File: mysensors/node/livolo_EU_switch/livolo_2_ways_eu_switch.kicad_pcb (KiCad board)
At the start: 2 copper layers, 43.4 x 43.5 mm, 50 parts, among them CON1 AVR-ISP-6, IC1 ATMEGA328P-AU, P1 Sense Pad 1, P2 Sense Pad 2, P3 ANTENNA, P4 Power Board, U1 MIC5205-3.3, U2 MCP16301, U3 TTP223, U4 TTP223, U5 RFM69CW, U6 AT25DF512C-SSHN-B, U7 ATSHA204A

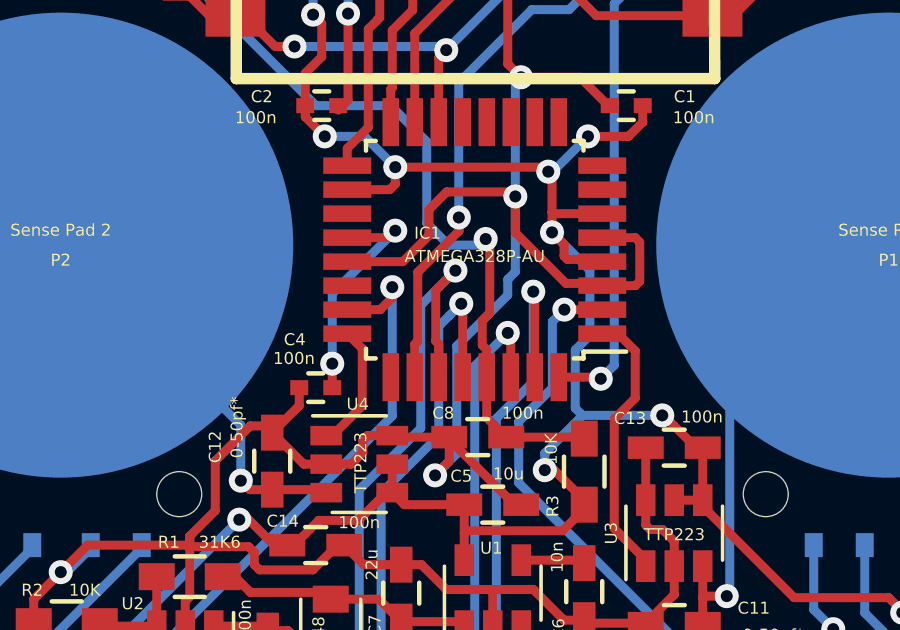
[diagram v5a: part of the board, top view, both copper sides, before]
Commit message: [livolo_EU_switch] cleaned up schematic
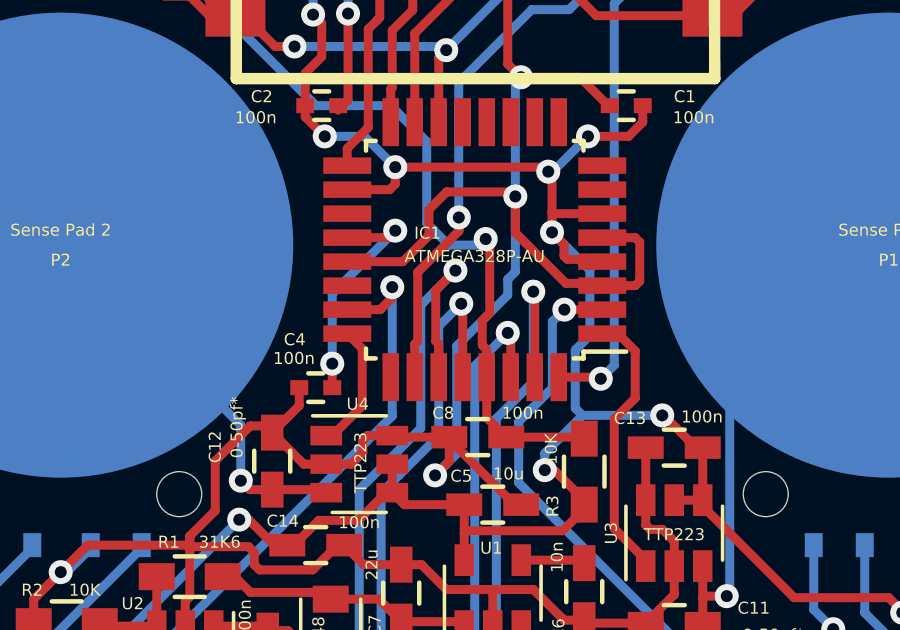
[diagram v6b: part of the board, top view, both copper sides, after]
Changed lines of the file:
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@@
     (thickness 1.6)
     (drawings 15)
-    (tracks 590)
+    (tracks 589)
     (zones 0)
     (modules 50)
@@
     (tags SOT-23-6)
     (attr smd)
-    (fp_text reference U2 (at -1.85 1.75 360) (layer F.SilkS)
+    (fp_text reference U2 (at -1.85 1.75) (layer F.SilkS)
       (effects (font (size 0.4 0.4) (thickness 0.1)))
     )
@@
   (gr_line (start 151.552777 113.515554) (end 131.572683 113.515554) (layer Edge.Cuts) (width 0.1))
   (gr_line (start 164.116018 81.426312) (end 164.116018 102.125387) (layer Edge.Cuts) (width 0.1))
-  (segment (start 146.7 92.7) (end 146.625001 92.625001) (width 0.3) (layer F.Cu) (net 1))
-  (segment (start 146.625001 92.625001) (end 145.539999 92.625001) (width 0.3) (layer F.Cu) (net 1))
+  (segment (start 146.7 92.7) (end 146.625001 92.625001) (width 0.3) (layer F.Cu) (net 1) (status 30))
+  (segment (start 146.625001 92.625001) (end 145.539999 92.625001) (width 0.3) (layer F.Cu) (net 1) (status 10))
   (segment (start 145.539999 92.625001) (end 145.426047 92.511049) (width 0.3) (layer F.Cu) (net 1))
   (segment (start 145.426047 92.511049) (end 145.426047 92.123951) (width 0.3) (layer F.Cu) (net 1))
@@
   (segment (start 137.250001 101.324999) (end 136.425 102.15) (width 0.3) (layer F.Cu) (net 1) (status 20))
   (segment (start 150.05 100.65) (end 150.05 98.9) (width 0.3) (layer F.Cu) (net 1) (status 30))
-  (segment (start 152.85 72.25) (end 152.15 72.25) (width 0.3) (layer F.Cu) (net 2))
-  (segment (start 152.15 72.25) (end 150.72104 72.25) (width 0.3) (layer F.Cu) (net 2))
+  (segment (start 152.85 72.25) (end 152.15 72.25) (width 0.3) (layer F.Cu) (net 2) (status 10))
+  (segment (start 152.15 72.25) (end 150.72104 72.25) (width 0.3) (layer F.Cu) (net 2) (status 20))
   (segment (start 154.7 77.600002) (end 152.15 75.050002) (width 0.3) (layer F.Cu) (net 2))
   (segment (start 152.15 75.050002) (end 152.15 72.25) (width 0.3) (layer F.Cu) (net 2))
-  (segment (start 145.491456 93.425001) (end 146.625001 93.425001) (width 0.3) (layer F.Cu) (net 2))
+  (segment (start 145.491456 93.425001) (end 146.625001 93.425001) (width 0.3) (layer F.Cu) (net 2) (status 20))
   (segment (start 143.802464 90.525717) (end 143.802464 91.736009) (width 0.3) (layer F.Cu) (net 2))
   (segment (start 143.802464 91.736009) (end 145.491456 93.425001) (width 0.3) (layer F.Cu) (net 2))
-  (segment (start 146.625001 93.425001) (end 146.7 93.5) (width 0.3) (layer F.Cu) (net 2))
+  (segment (start 146.625001 93.425001) (end 146.7 93.5) (width 0.3) (layer F.Cu) (net 2) (status 30))
   (segment (start 147.950001 92.050001) (end 147.950001 93.349999) (width 0.3) (layer F.Cu) (net 2))
   (segment (start 147.950001 93.349999) (end 147.8 93.5) (width 0.3) (layer F.Cu) (net 2))
-  (segment (start 146.7 93.5) (end 147.8 93.5) (width 0.3) (layer F.Cu) (net 2))
+  (segment (start 146.7 93.5) (end 147.8 93.5) (width 0.3) (layer F.Cu) (net 2) (status 10))
   (segment (start 147.8 91.9) (end 147.950001 92.050001) (width 0.3) (layer F.Cu) (net 2))
   (segment (start 146.7 91.9) (end 147.8 91.9) (width 0.3) (layer F.Cu) (net 2) (status 10))
-  (segment (start 138.2 92.7) (end 140.053139 92.7) (width 0.3) (layer F.Cu) (net 2))
+  (segment (start 138.2 92.7) (end 140.053139 92.7) (width 0.3) (layer F.Cu) (net 2) (status 10))
   (segment (start 140.053139 92.7) (end 140.925 91.828139) (width 0.3) (layer F.Cu) (net 2))
   (segment (start 140.925 91.828139) (end 140.925 90.963954) (width 0.3) (layer F.Cu) (net 2))
@@
   (segment (start 137.65 103.95) (end 139.25 103.95) (width 0.3) (layer F.Cu) (net 5) (status 10))
   (segment (start 139.25 103.95) (end 140 104.7) (width 0.3) (layer F.Cu) (net 5) (status 20))
-  (segment (start 142.85 96.55) (end 142.85 95.632681) (width 0.3) (layer F.Cu) (net 6))
+  (segment (start 142.85 96.55) (end 142.85 95.632681) (width 0.3) (layer F.Cu) (net 6) (status 10))
   (segment (start 142.85 95.632681) (end 142.699989 95.48267) (width 0.3) (layer F.Cu) (net 6))
   (segment (start 142.699989 95.48267) (end 142.699989 94.664027) (width 0.3) (layer F.Cu) (net 6))
@@
   (segment (start 135.7 100.3) (end 137.4 100.3) (width 0.3) (layer F.Cu) (net 11) (status 30))
   (segment (start 137.4 100.3) (end 137.5 100.4) (width 0.3) (layer F.Cu) (net 11) (status 30))
-  (segment (start 154.415 79.5) (end 154.415 80.575) (width 0.3) (layer F.Cu) (net 12))
-  (segment (start 151.07378 84.50122) (end 150.37226 84.50122) (width 0.3) (layer F.Cu) (net 12))
+  (segment (start 154.415 79.5) (end 154.415 80.575) (width 0.3) (layer F.Cu) (net 12) (status 10))
+  (segment (start 151.07378 84.50122) (end 150.37226 84.50122) (width 0.3) (layer F.Cu) (net 12) (status 30))
   (segment (start 154.415 80.575) (end 154.250001 80.739999) (width 0.3) (layer F.Cu) (net 12))
   (segment (start 154.250001 80.739999) (end 154.250001 82.510001) (width 0.3) (layer F.Cu) (net 12))
   (segment (start 154.250001 82.510001) (end 153.860002 82.9) (width 0.3) (layer F.Cu) (net 12))
   (segment (start 153.860002 82.9) (end 152.675 82.9) (width 0.3) (layer F.Cu) (net 12))
-  (segment (start 152.675 82.9) (end 151.07378 84.50122) (width 0.3) (layer F.Cu) (net 12))
+  (segment (start 152.675 82.9) (end 151.07378 84.50122) (width 0.3) (layer F.Cu) (net 12) (status 20))
   (segment (start 128.450018 81.600004) (end 128.000012 82.05001) (width 0.3) (layer B.Cu) (net 12))
   (segment (start 129.55001 82.05001) (end 128.000012 82.05001) (width 0.3) (layer F.Cu) (net 12) (status 10))
@@
   (segment (start 144.45 93.75) (end 144.4 93.7) (width 0.3) (layer F.Cu) (net 28))
   (via (at 144.4 93.7) (size 0.8) (drill 0.4) (layers F.Cu B.Cu) (net 28))
-  (segment (start 141.249969 94.853552) (end 141.600036 94.503485) (width 0.3) (layer B.Cu) (net 29))
+  (segment (start 141.249969 94.853552) (end 142.000035 94.103486) (width 0.3) (layer B.Cu) (net 29))
   (segment (start 142.05 94.153451) (end 142.000035 94.103486) (width 0.3) (layer F.Cu) (net 29))
-  (segment (start 141.600036 94.503485) (end 142.000035 94.103486) (width 0.3) (layer B.Cu) (net 29))
   (segment (start 141.249969 98.500031) (end 141.249969 94.853552) (width 0.3) (layer B.Cu) (net 29))
   (segment (start 139.329999 100.420001) (end 141.249969 98.500031) (width 0.3) (layer B.Cu) (net 29))
   (segment (start 139.329999 108.749999) (end 139.329999 100.420001) (width 0.3) (layer B.Cu) (net 29))
   (via (at 142.000035 94.103486) (size 0.8) (drill 0.4) (layers F.Cu B.Cu) (net 29))
-  (segment (start 140.63 110.05) (end 139.329999 108.749999) (width 0.3) (layer B.Cu) (net 29))
-  (segment (start 142.05 96.55) (end 142.05 94.153451) (width 0.3) (layer F.Cu) (net 29))
+  (segment (start 140.63 110.05) (end 139.329999 108.749999) (width 0.3) (layer B.Cu) (net 29) (status 10))
+  (segment (start 142.05 96.55) (end 142.05 94.153451) (width 0.3) (layer F.Cu) (net 29) (status 10))
   (segment (start 141.150025 93.653754) (end 141.150025 95.350025) (width 0.3) (layer F.Cu) (net 30))
-  (segment (start 141.25 95.45) (end 141.25 96.55) (width 0.3) (layer F.Cu) (net 30))
+  (segment (start 141.25 95.45) (end 141.25 96.55) (width 0.3) (layer F.Cu) (net 30) (status 20))
   (segment (start 141.150025 95.350025) (end 141.25 95.45) (width 0.3) (layer F.Cu) (net 30))
   (segment (start 140.649958 94.153821) (end 141.805637 92.998142) (width 0.3) (layer B.Cu) (net 30))
@@
   (segment (start 141.150025 93.653754) (end 141.805637 92.998142) (width 0.3) (layer F.Cu) (net 30))
   (via (at 141.805637 92.998142) (size 0.8) (drill 0.4) (layers F.Cu B.Cu) (net 30))
-  (segment (start 140.45 96.55) (end 140.45 95.45) (width 0.3) (layer F.Cu) (net 31))
+  (segment (start 140.45 96.55) (end 140.45 95.45) (width 0.3) (layer F.Cu) (net 31) (status 10))
   (segment (start 140.45 95.45) (end 140.550013 95.349987) (width 0.3) (layer F.Cu) (net 31))
   (segment (start 140.550014 93.051668) (end 141.925 91.676682) (width 0.3) (layer F.Cu) (net 31))

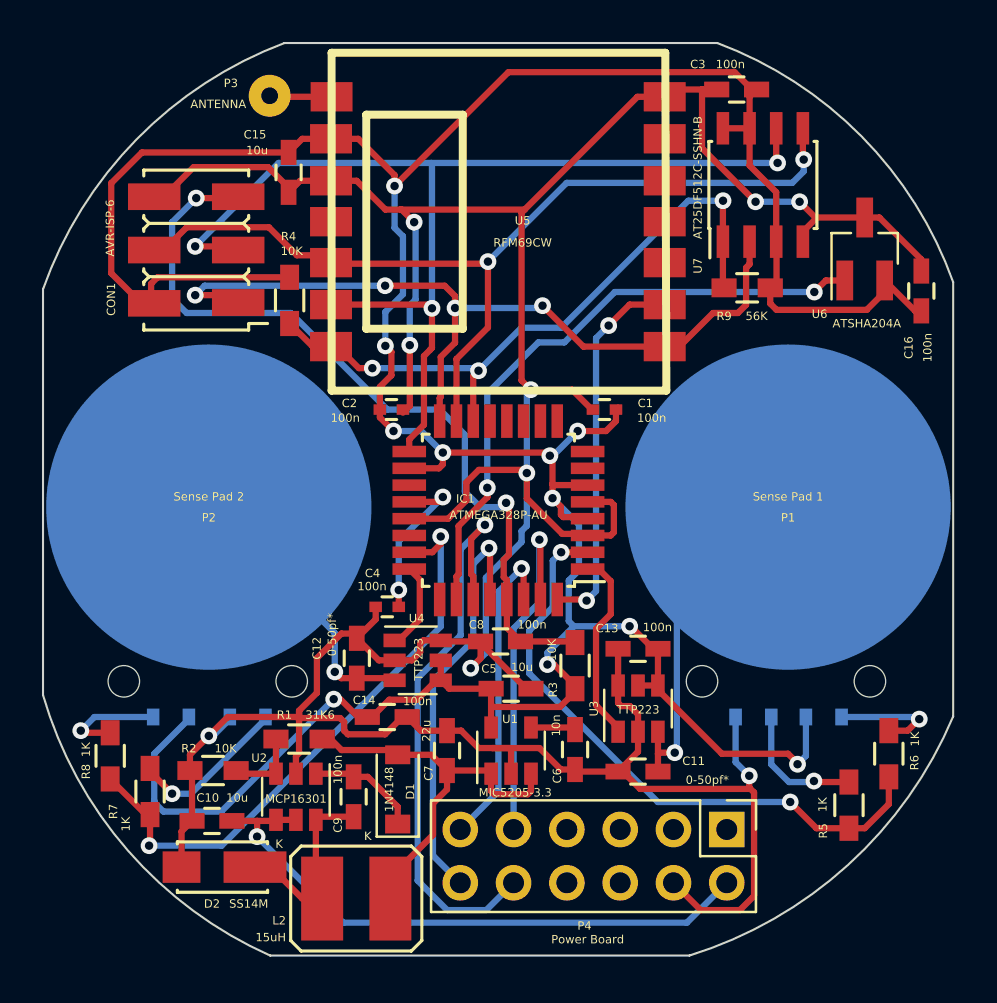
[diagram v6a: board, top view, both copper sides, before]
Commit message: [livolo_EU_switch] added gerber files and fixed board frame
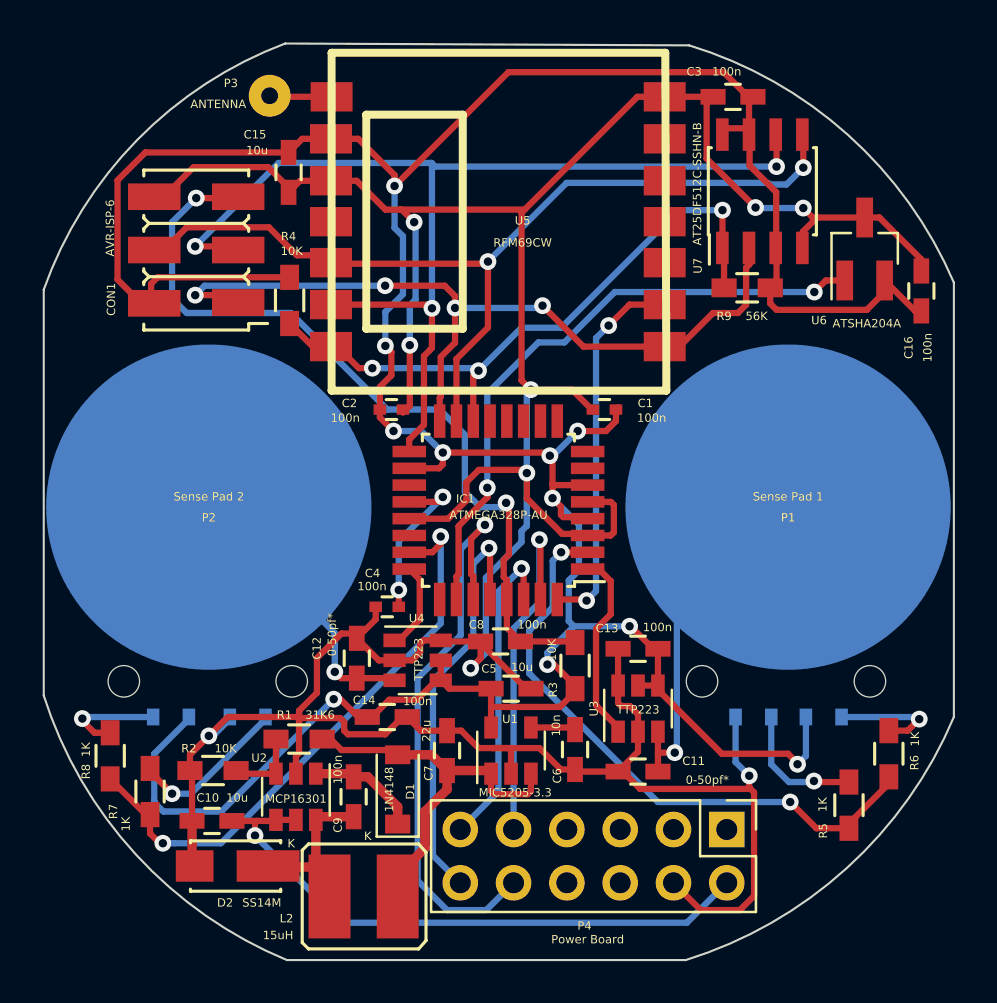
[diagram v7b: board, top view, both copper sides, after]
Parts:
- moved REF** 0.64 mm to (143.1, 92.0)
- moved D2 0.63 mm to (129.5, 109.2)
- moved C3 0.39 mm to (153.6, 72.6)
- moved L2 0.36 mm to (135.9, 110.7)
- moved U6 0.30 mm to (155.0, 77.1)
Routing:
- net Net-(C9-Pad2): track 9.13 -> 10.1 mm
- net /SS: track 31.6 -> 31.0 mm
- net /S2_LEDs: track 28.6 -> 28.0 mm
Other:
- board size 43.4 x 43.5 mm -> 43.4 x 43.7 mm

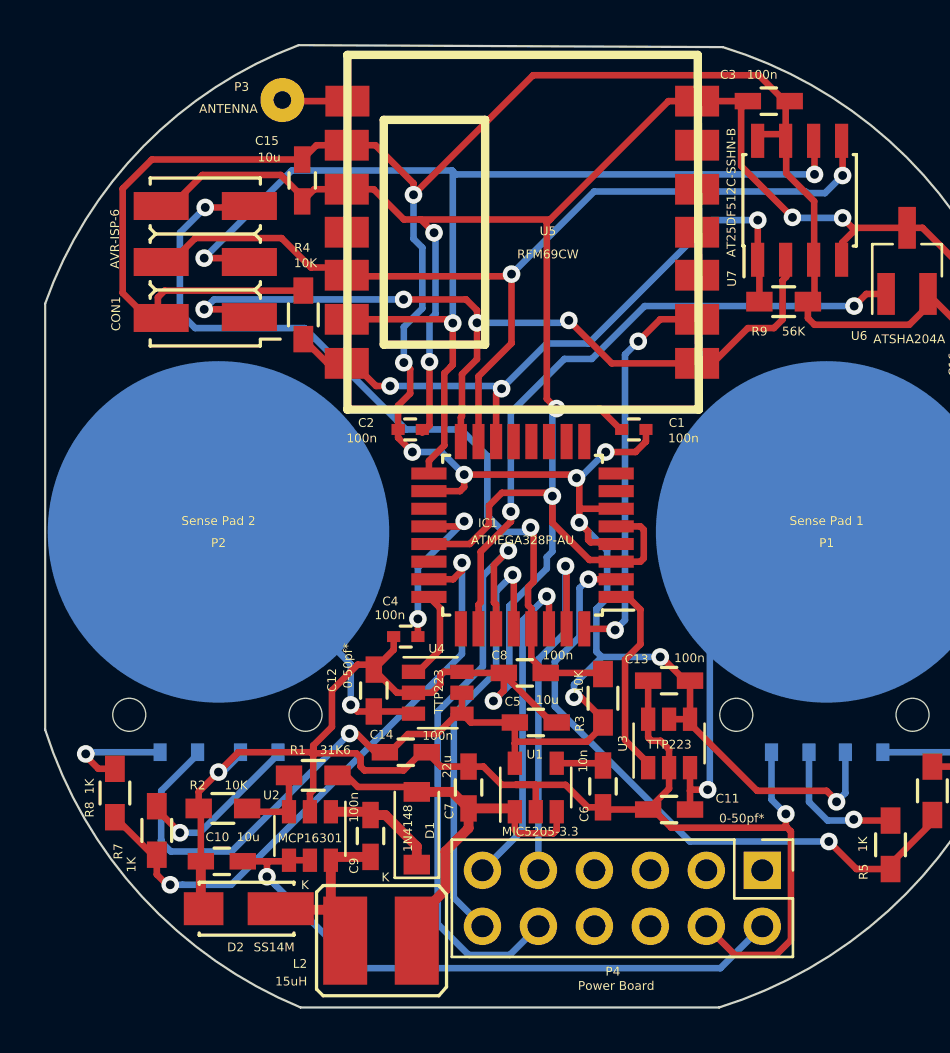
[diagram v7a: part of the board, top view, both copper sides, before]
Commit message: [livolo_EU_switch] some board touches
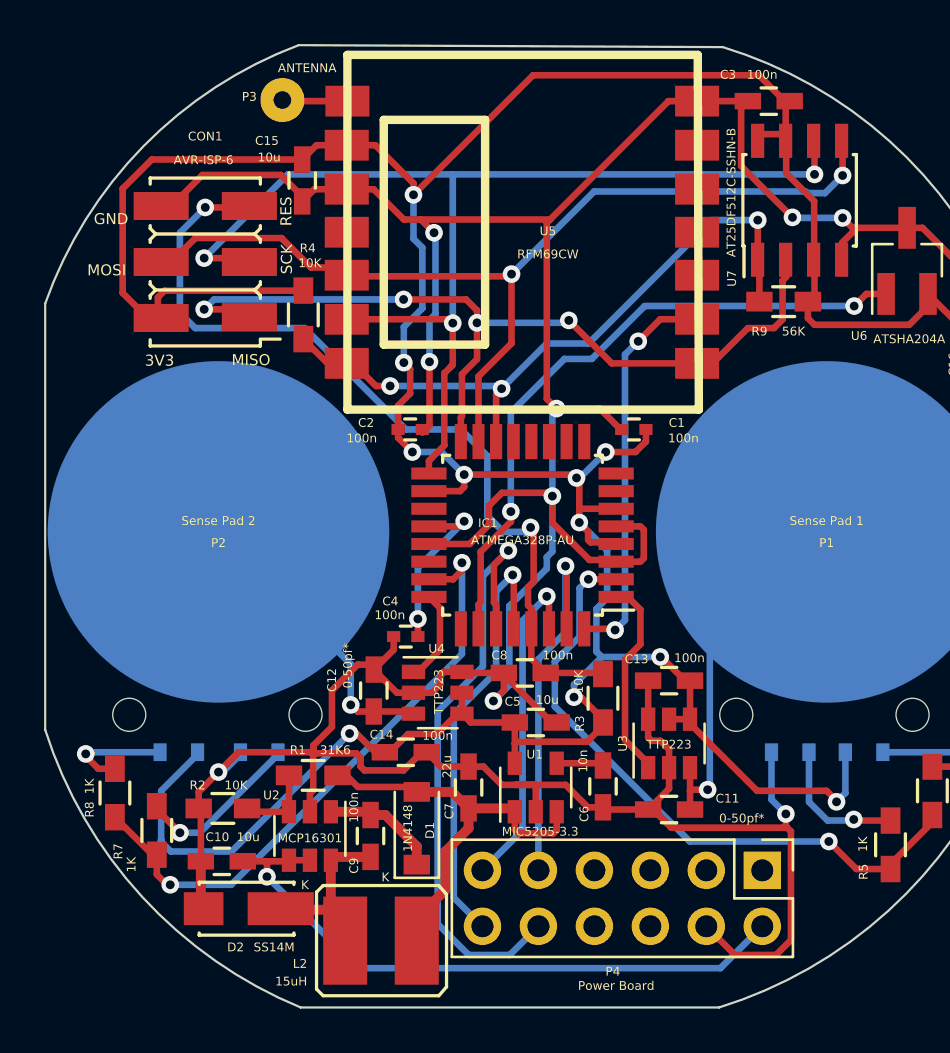
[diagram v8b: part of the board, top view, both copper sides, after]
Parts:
- added REF**: my_logo, myfootprints:my_logo, B.Cu at (142.4, 100.2)
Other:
- board text added: "12V"
- board text added: "3V3"
- board text added: "GND"
- board text added: "MISO"
- board text added: "MOSI"
- board text added: "Mysensors RFM69CW Livolo Node"
- board text added: "RES"
- board text added: "SCK"
